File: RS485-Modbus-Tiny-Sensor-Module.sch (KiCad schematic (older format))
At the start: 10 parts, among them SW1 FSM4JSMA, U2 ATtiny3216-S

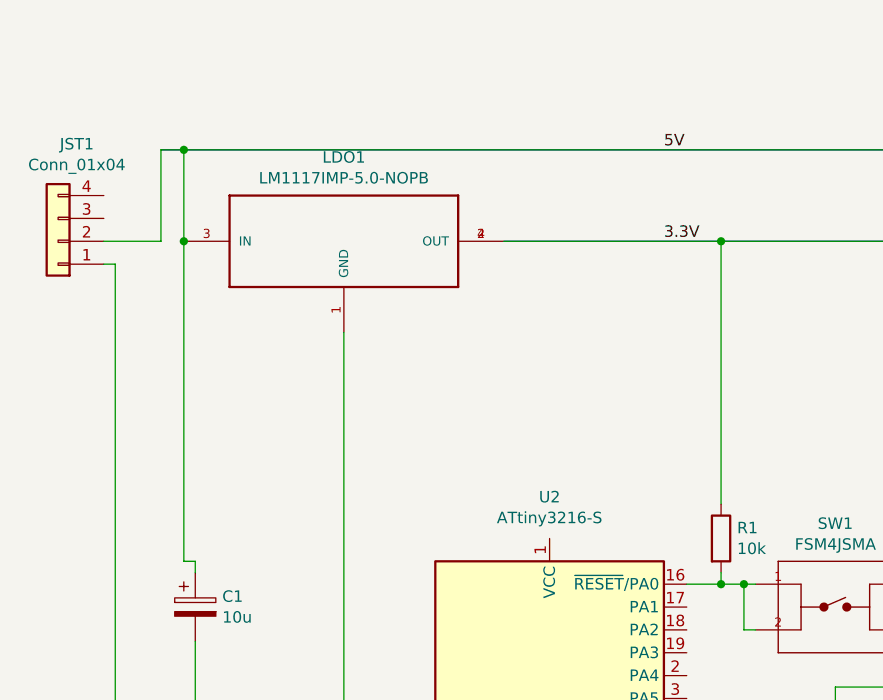
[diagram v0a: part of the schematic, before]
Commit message: Add files via upload
Changed JST connection to smallest + fix connection to 3.3 V
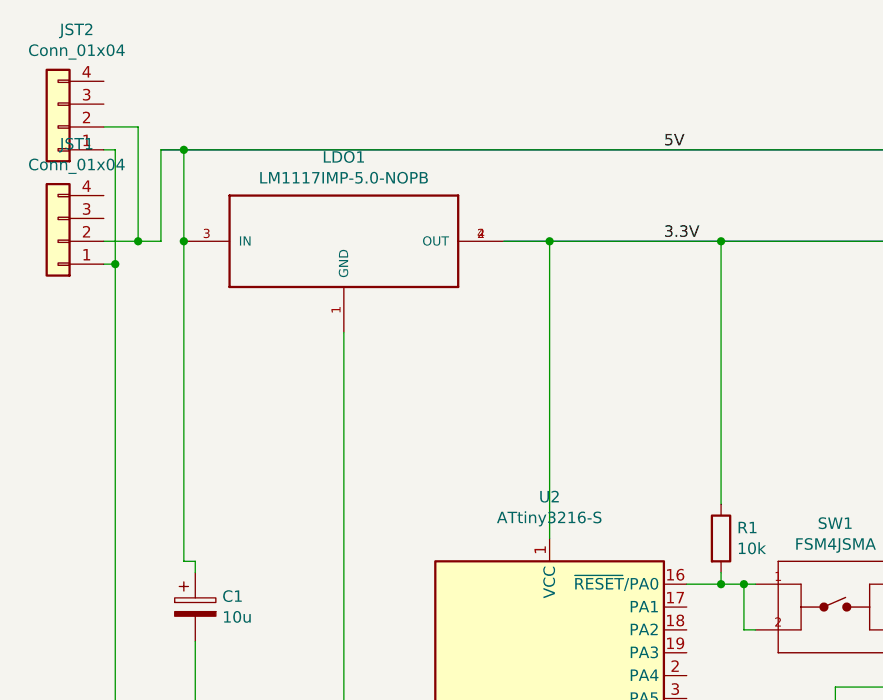
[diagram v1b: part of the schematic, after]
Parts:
- added JST2: Conn_01x04, Connector_JST:JST_SH_BM04B-SRSS-TB_1x04-1MP_P1.00mm_Vertical, symbol Connector_Generic:Conn_01x04
- JST1: footprint Connector_JST:JST_PH_B4B-PH-K_1x04_P2.00mm_Vertical -> Connector_JST:JST_SH_BM04B-SRSS-TB_1x04-1MP_P1.00mm_Vertical
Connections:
- wire segments 40 -> 47
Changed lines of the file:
@@
 	4550 3650 4300 3650
 Wire Bus Line
-	2550 1600 3500 1600
+	2550 1600 2750 1600
 Text Label 3250 1600 0    50   ~ 0
 3.3V
@@
 	1    5000 3250
 	1    0    0    -1
-$EndComp
-$Comp
-L Connector_Generic:Conn_01x04 JST1
-U 1 1 5E82DEC1
-P 600 1600
-F 0 "JST1" H 518 1175 50  0000 C CNN
-F 1 "Conn_01x04" H 518 1266 50  0000 C CNN
-F 2 "Connector_JST:JST_PH_B4B-PH-K_1x04_P2.00mm_Vertical" H 600 1600 50  0001 C CNN
-F 3 "~" H 600 1600 50  0001 C CNN
-	1    600  1600
-	-1   0    0    1
 $EndComp
 Text Label 3600 4950 0    50   ~ 0
@@
 	850  1700 850  4950
 Wire Wire Line
-	800  1600 1050 1600
+	800  1600 950  1600
 Wire Wire Line
 	1050 1600 1050 1200
@@
 	1150 1200 5350 1200
 Wire Wire Line
-	2550 1600 3500 1600
+	2550 1600 2750 1600
 Connection ~ 3500 1600
 Wire Bus Line
@@
 Wire Bus Line
 	5000 4950 6300 4950
+Wire Wire Line
+	2750 1600 2750 2900
+Connection ~ 2750 1600
+Wire Bus Line
+	2750 1600 3500 1600
+Wire Wire Line
+	2750 1600 3500 1600
+$Comp
+L Connector_Generic:Conn_01x04 JST1
+U 1 1 5E82DEC1
+P 600 1600
+F 0 "JST1" H 518 1175 50  0000 C CNN
+F 1 "Conn_01x04" H 518 1266 50  0000 C CNN
+F 2 "Connector_JST:JST_SH_BM04B-SRSS-TB_1x04-1MP_P1.00mm_Vertical" H 600 1600 50  0001 C CNN
+F 3 "~" H 600 1600 50  0001 C CNN
+	1    600  1600
+	-1   0    0    1
+$EndComp
+$Comp
+L Connector_Generic:Conn_01x04 JST2
+U 1 1 5E7FDED7
+P 600 1100
+F 0 "JST2" H 518 675 50  0000 C CNN
+F 1 "Conn_01x04" H 518 766 50  0000 C CNN
+F 2 "Connector_JST:JST_SH_BM04B-SRSS-TB_1x04-1MP_P1.00mm_Vertical" H 600 1100 50  0001 C CNN
+F 3 "~" H 600 1100 50  0001 C CNN
+	1    600  1100
+	-1   0    0    1
+$EndComp
+Connection ~ 950  1600
+Wire Wire Line
+	950  1600 1050 1600
+Wire Wire Line
+	950  1100 800  1100
+Wire Wire Line
+	950  1100 950  1600
+Wire Wire Line
+	800  1200 850  1200
+Wire Wire Line
+	850  1200 850  1700
+Connection ~ 850  1700
 $EndSCHEMATC

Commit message: Add files via upload
Added 24V LDO + cleaned layout + added autoreset
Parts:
- removed C3: 2700u, Capacitor_THT:CP_Radial_D12.5mm_P5.00mm, symbol Device:CP
- removed LDO1: LM1117IMP-5.0-NOPB, SOT223, symbol LM1117IMP-5.0-NOPB:LM1117IMP-5.0-NOPB
- added C3: 100u, Capacitor_SMD:C_1206_3216Metric, symbol Device:C
- added C4: 100u, Capacitor_SMD:CP_Elec_6.3x7.7, symbol Device:CP
- added C5: 10u, Capacitor_SMD:C_1206_3216Metric, symbol Device:C
- added D2: D, Diode_SMD:D_1206_3216Metric_Pad1.42x1.75mm_HandSolder, symbol Device:D
- added J1: Conn_01x06, Connector_JST:JST_EH_B6B-EH-A_1x06_P2.50mm_Vertical, symbol Connector_Generic:Conn_01x06
- added JST3: Conn_01x03, Connector_JST:JST_SH_BM03B-SRSS-TB_1x03-1MP_P1.00mm_Vertical, symbol Connector_Generic:Conn_01x03
- added LDO1: LD1086DT50TR, Package_TO_SOT_SMD:TO-252-2, symbol Regulator_Linear:LD1086DT50TR
- added LDO2: MIC5504-3.3YM5, Package_TO_SOT_SMD:SOT-23-5, symbol Regulator_Linear:MIC5504-3.3YM5
- C1: value 10u -> 100u; symbol Device:CP -> Device:C
- C2: symbol Device:CP -> Device:C
- R2: value 200 -> 300
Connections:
- net labels added: 24V, DTR, PA7, RX, TX
- wire segments 47 -> 78
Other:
- moved on the sheet: D1, JST1, JST2, R2

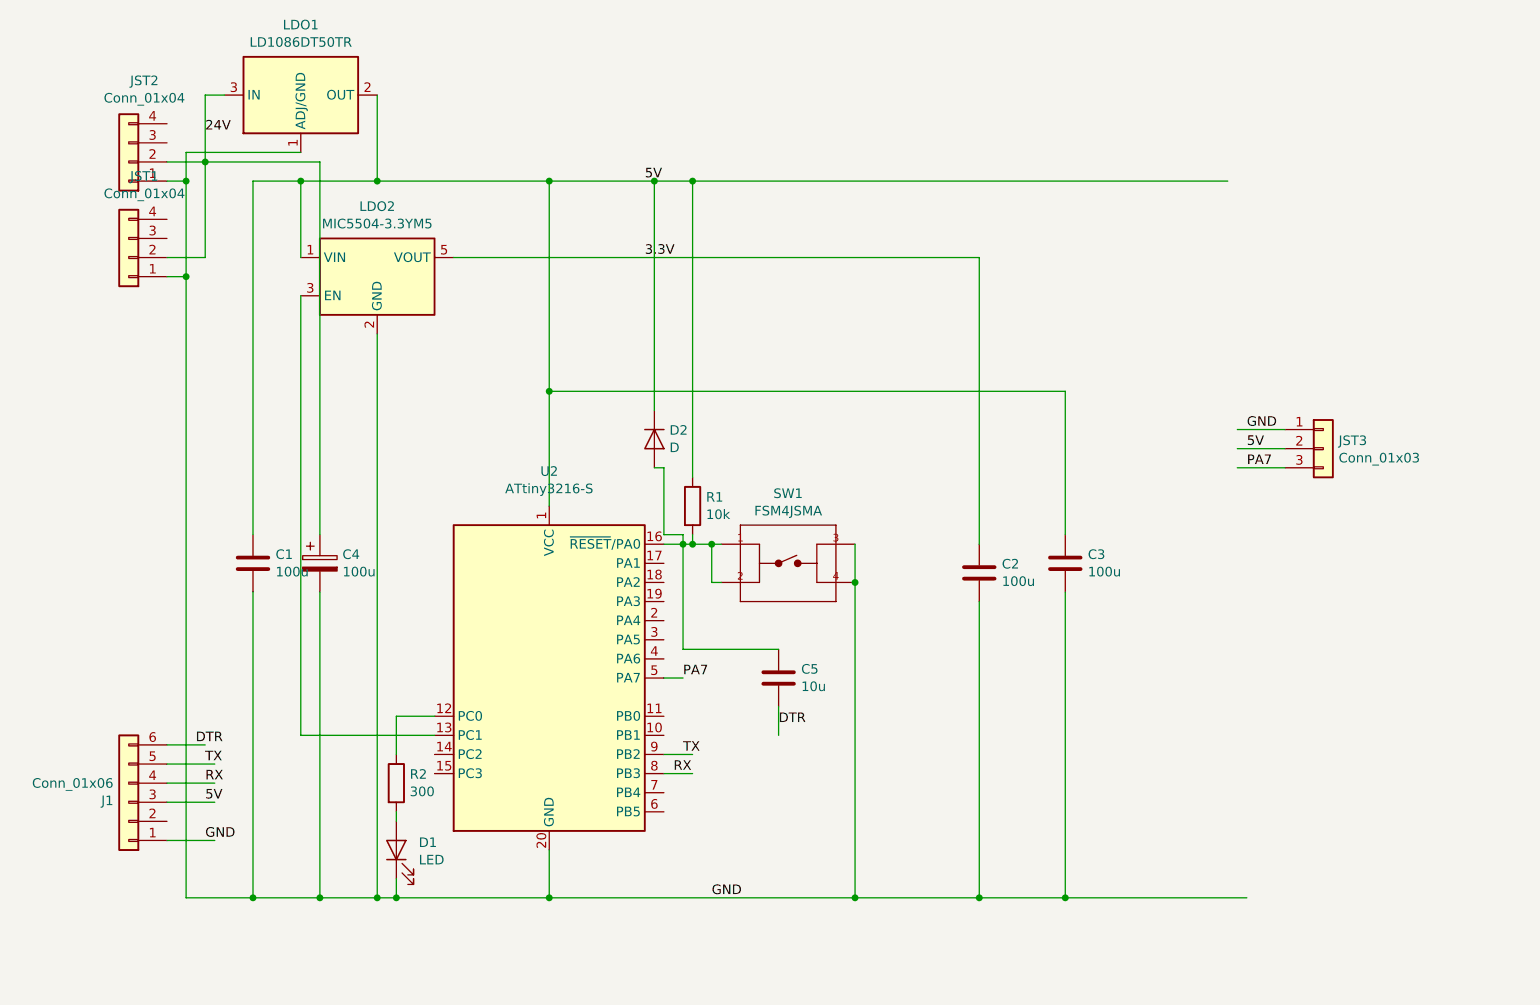
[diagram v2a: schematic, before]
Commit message: Add files via upload
Finished layout prototype + added extra JST
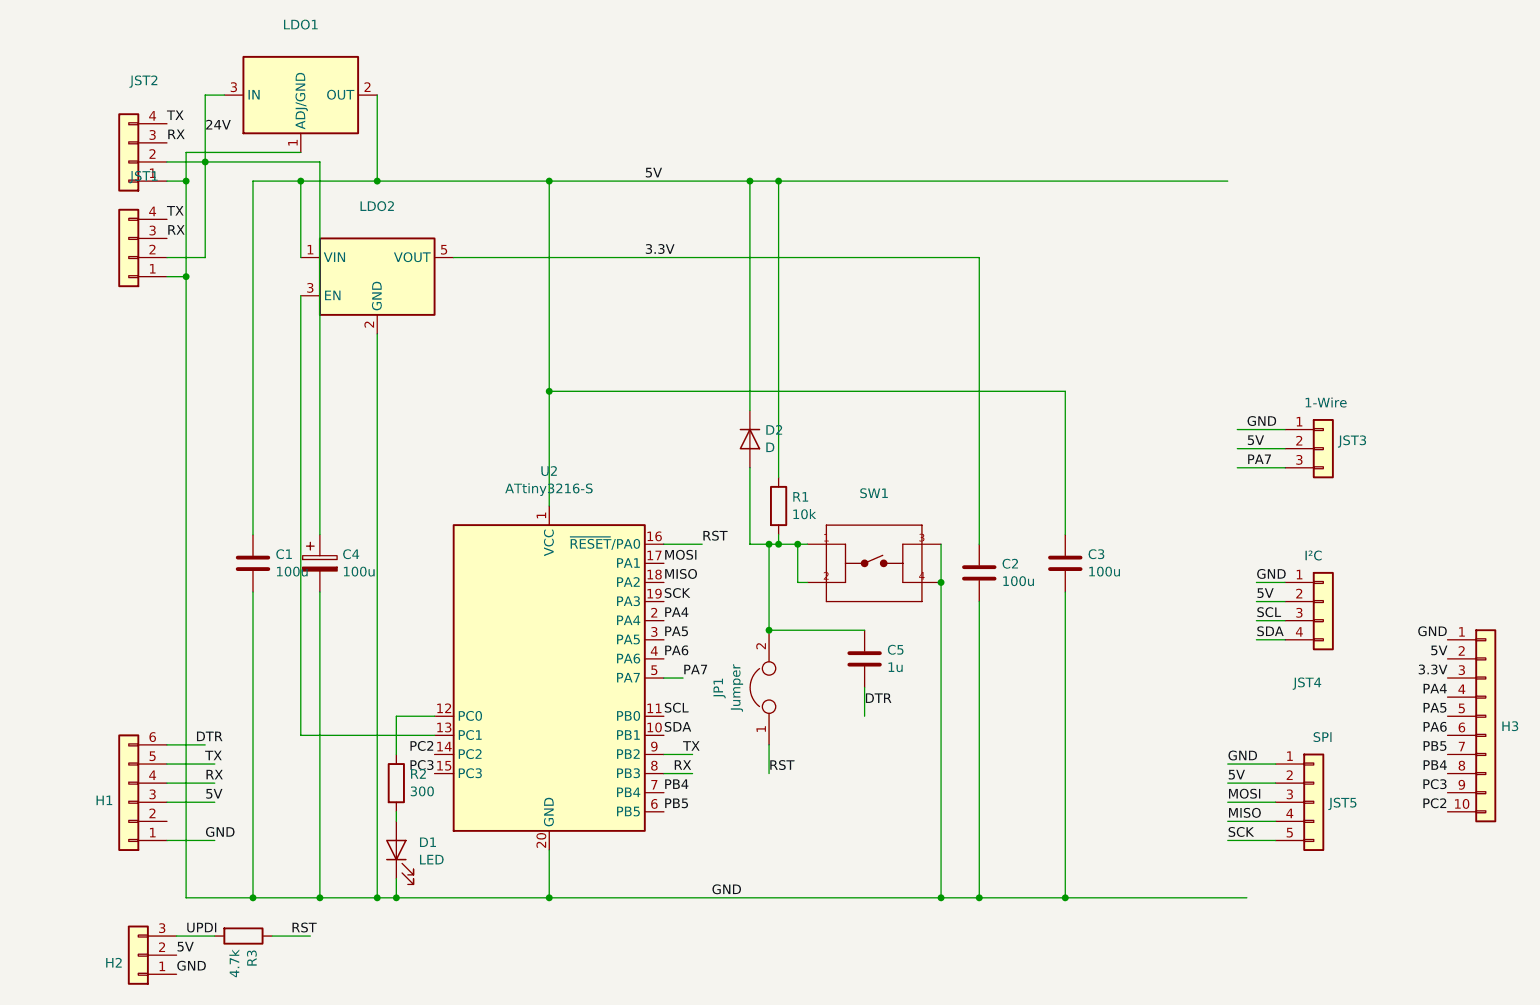
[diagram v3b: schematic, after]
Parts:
- added H2: Conn_01x03, Connector_PinHeader_2.00mm:PinHeader_1x03_P2.00mm_Vertical, symbol Connector_Generic:Conn_01x03
- added H3: Conn_01x10, Connector_PinHeader_2.00mm:PinHeader_1x10_P2.00mm_Vertical, symbol Connector_Generic:Conn_01x10
- added JP1: Jumper, Jumper:SolderJumper-2_P1.3mm_Open_Pad1.0x1.5mm, symbol Device:Jumper
- added JST4: Conn_01x04, Connector_JST:JST_SH_BM04B-SRSS-TB_1x04-1MP_P1.00mm_Vertical, symbol Connector_Generic:Conn_01x04
- added JST5: Conn_01x05, Connector_JST:JST_SH_BM05B-SRSS-TB_1x05-1MP_P1.00mm_Vertical, symbol Connector_Generic:Conn_01x05
- added R3: 4.7k, Resistor_SMD:R_1206_3216Metric, symbol Device:R
- C5: value 10u -> 1u
- H1: renamed from J1; footprint Connector_JST:JST_EH_B6B-EH-A_1x06_P2.50mm_Vertical -> Connector_PinHeader_2.00mm:PinHeader_1x06_P2.00mm_Vertical
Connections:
- net labels added: MISO, MOSI, PA4, PA5, PA6, PB4, PB5, PC2, PC3, RST, SCK, SCL, SDA, UPDI
- wire segments 78 -> 88
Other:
- note added: "1-Wire"
- note added: "I²C"
- note added: "SPI"
- moved on the sheet: C5, D2, R1, SW1

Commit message: Add files via upload
Added BOM + .zip file that contains files for production of PCB
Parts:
- JP1: footprint Jumper:SolderJumper-2_P1.3mm_Open_Pad1.0x1.5mm -> Resistor_SMD:R_0805_2012Metric
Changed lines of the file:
@@
 F 0 "JP1" H 3900 4114 50  0000 C CNN
 F 1 "Jumper" H 3900 4023 50  0000 C CNN
-F 2 "Jumper:SolderJumper-2_P1.3mm_Open_Pad1.0x1.5mm" H 3900 3850 50  0001 C CNN
+F 2 "Resistor_SMD:R_0805_2012Metric" H 3900 3850 50  0001 C CNN
 F 3 "~" H 3900 3850 50  0001 C CNN
 	1    3900 3850

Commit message: Add files via upload
PCB V1.0
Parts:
- removed C5: 1u, Capacitor_SMD:C_1206_3216Metric, symbol Device:C
- removed D2: D, Diode_SMD:D_1206_3216Metric_Pad1.42x1.75mm_HandSolder, symbol Device:D
- removed H1: Conn_01x06, Connector_PinHeader_2.00mm:PinHeader_1x06_P2.00mm_Vertical, symbol Connector_Generic:Conn_01x06
- removed H2: Conn_01x03, Connector_PinHeader_2.00mm:PinHeader_1x03_P2.00mm_Vertical, symbol Connector_Generic:Conn_01x03
- removed JP1: Jumper, Resistor_SMD:R_0805_2012Metric, symbol Device:Jumper
- removed R1: 10k, Resistor_SMD:R_1206_3216Metric, symbol Device:R
- removed SW1: FSM4JSMA, TE_FSM4JSMA, symbol FSM4JSMA:FSM4JSMA
- added UPDI1: Conn_01x03, Connector_JST:JST_SH_SM03B-SRSS-TB_1x03-1MP_P1.00mm_Horizontal, symbol Connector_Generic:Conn_01x03
- 1-Wire1: renamed from JST3; footprint Connector_JST:JST_SH_BM03B-SRSS-TB_1x03-1MP_P1.00mm_Vertical -> Connector_JST:JST_SH_SM03B-SRSS-TB_1x03-1MP_P1.00mm_Horizontal
- H1: renamed from H3; footprint Connector_PinHeader_2.00mm:PinHeader_1x10_P2.00mm_Vertical -> Connector_PinHeader_2.54mm:PinHeader_1x10_P2.54mm_Vertical
- I²C1: renamed from JST4; footprint Connector_JST:JST_SH_BM04B-SRSS-TB_1x04-1MP_P1.00mm_Vertical -> Connector_JST:JST_SH_SM04B-SRSS-TB_1x04-1MP_P1.00mm_Horizontal
- RS485: renamed from JST1; footprint Connector_JST:JST_SH_BM04B-SRSS-TB_1x04-1MP_P1.00mm_Vertical -> Connector_JST:JST_SH_SM04B-SRSS-TB_1x04-1MP_P1.00mm_Horizontal
- RS485_2: renamed from JST2; footprint Connector_JST:JST_SH_BM04B-SRSS-TB_1x04-1MP_P1.00mm_Vertical -> Connector_JST:JST_SH_SM04B-SRSS-TB_1x04-1MP_P1.00mm_Horizontal
- SPI1: renamed from JST5; value Conn_01x05 -> Conn_01x06; footprint Connector_JST:JST_SH_BM05B-SRSS-TB_1x05-1MP_P1.00mm_Vertical -> Connector_JST:JST_SH_SM06B-SRSS-TB_1x06-1MP_P1.00mm_Horizontal; symbol Connector_Generic:Conn_01x05 -> Connector_Generic:Conn_01x06
- renumbered R2 to R1, R3 to R2
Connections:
- net labels removed: DTR, UPDI
- wire segments 88 -> 64
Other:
- note removed: "1-Wire"
- note removed: "I²C"
- note removed: "SPI"
- moved on the sheet: 1-Wire1, C3, R2
